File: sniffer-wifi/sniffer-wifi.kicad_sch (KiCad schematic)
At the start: 23 parts, among them J1 Conn_01x05_Pin, J2 Screw_Terminal_01x02, J3 Screw_Terminal_01x02, Q1 BC547, Q2 BC547, Q3 BC547, U1 ESP-12E

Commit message: change schematics
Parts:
- removed J1: Conn_01x05_Pin, Connector_PinHeader_2.54mm:PinHeader_1x05_P2.54mm_Vertical, symbol Connector:Conn_01x05_Pin
- removed Q1, Q2: BC547, Package_TO_SOT_THT:TO-92, symbol Simulation_SPICE:NPN
- added C1: 100n, symbol Device:C
- added C2: 10u, symbol Device:C_Polarized
- added D2, D5: 1N4148, symbol Device:D
- added D3, D4: LED, LED_THT:LED_D3.0mm, symbol Device:LED
- added J1: USB_B_Micro, Connector_USB:USB_Micro-AB_Molex_47590-0001, symbol Connector:USB_B_Micro
- added J5: Conn_01x03_Pin, Connector_PinSocket_2.54mm:PinSocket_1x03_P2.54mm_Vertical, symbol Connector:Conn_01x03_Pin
- added JP1: Jumper_2_Open, TestPoint:TestPoint_2Pads_Pitch5.08mm_Drill1.3mm, symbol Jumper:Jumper_2_Open
- added R16: 1k, symbol Device:R
- added R17: 100, Resistor_THT:R_Axial_DIN0207_L6.3mm_D2.5mm_P7.62mm_Horizontal, symbol Device:R
- added SW1: SW_SPST, Button_Switch_THT:SW_PUSH_6mm_H5mm, symbol Switch:SW_SPST
- added U2: LF33_TO220, Package_TO_SOT_THT:TO-220-3_Vertical, symbol Regulator_Linear:LF33_TO220
- R12, R13: value 10k -> 1k; footprint (none) -> Resistor_THT:R_Axial_DIN0207_L6.3mm_D2.5mm_P7.62mm_Horizontal
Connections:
- net +3V3: now also C2.1, D3.2 (A), D4.2 (A), D5.2 (A), U2.3 (VO); no longer R15.2
- net BOOT: now also JP1.2 (B)
- net GND: now also C1.2, C2.2, D2.2 (A), J1.5 (GND), J1.6 (Shield), J5.3 (Pin_3), JP1.1 (A), SW1.1 (A), U2.2 (GND)
- net L+: now also R17.2; no longer Q3.3 (E)
- net L+TTL: now also D2.1 (K), R16.1; no longer Q3.1 (C), R14.2
- net RESET: now also SW1.2 (B)
- net RX: now also J5.2 (Pin_2)
- net TX: now also J5.1 (Pin_1)
- net STATUS_RED: now reaches R13.2
- net STATUS_RED: now also U1.7 (GPIO13)
- net STATUS_GREEN: now reaches R12.2
- net STATUS_GREEN: now also U1.6 (GPIO12)
- net DTR: no longer names the net of R12.1
- net DTR: now also D3.1 (K)
- net RTS: no longer names the net of R13.1
- net RTS: now also D4.1 (K)
- new net: Q3.1 (C), R14.2, R16.2
- new net: Q3.3 (E), R17.1
- new net: D5.1 (K), R15.2
- new net +5V: C1.1, J1.1 (VBUS), U2.1 (VI)
- no-connect marks 0 -> 4
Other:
- moved on the sheet: Q3, R14, R15

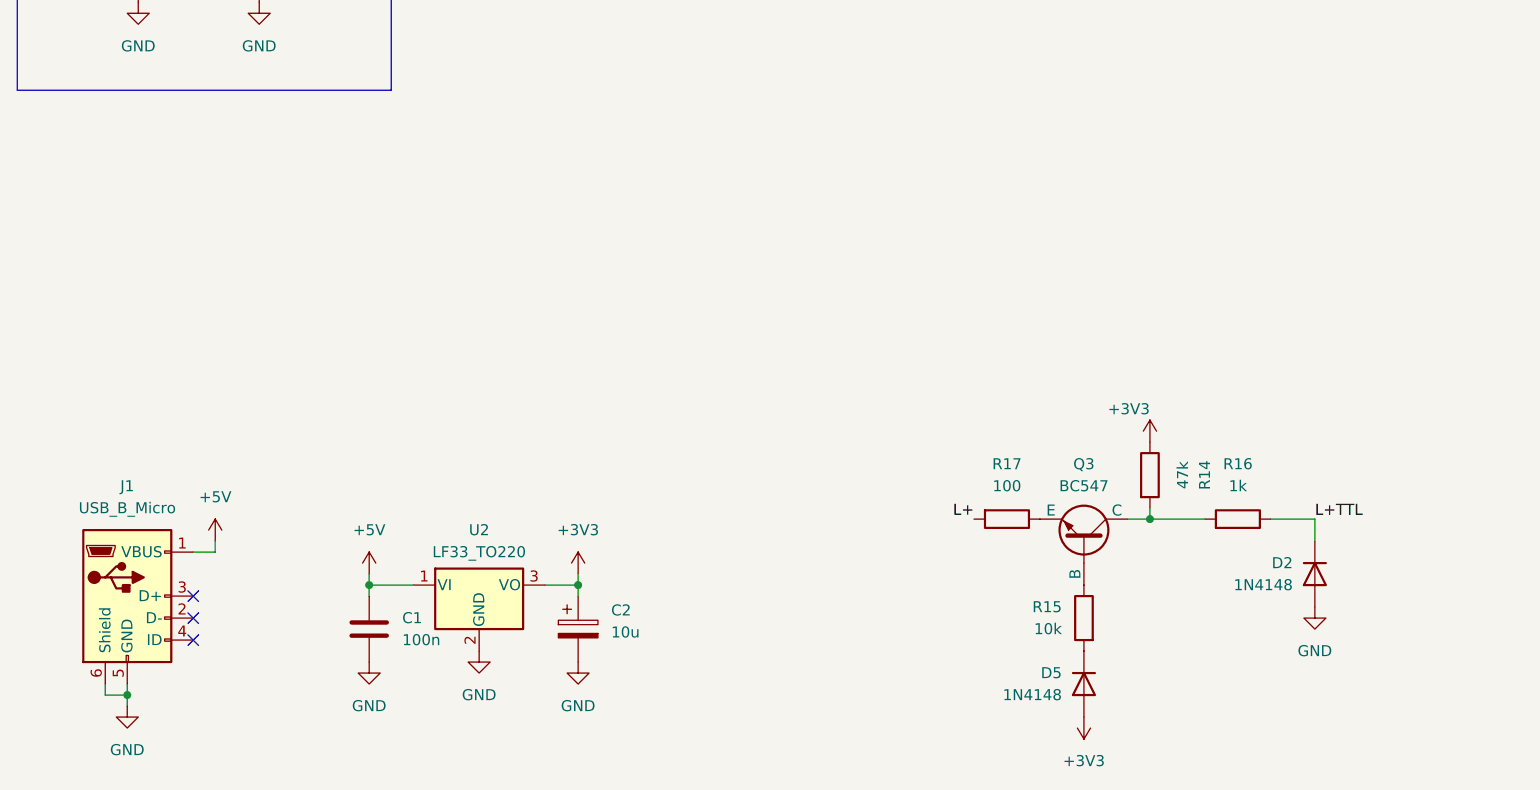
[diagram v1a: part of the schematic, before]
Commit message: modify L+ to LVTTL converter
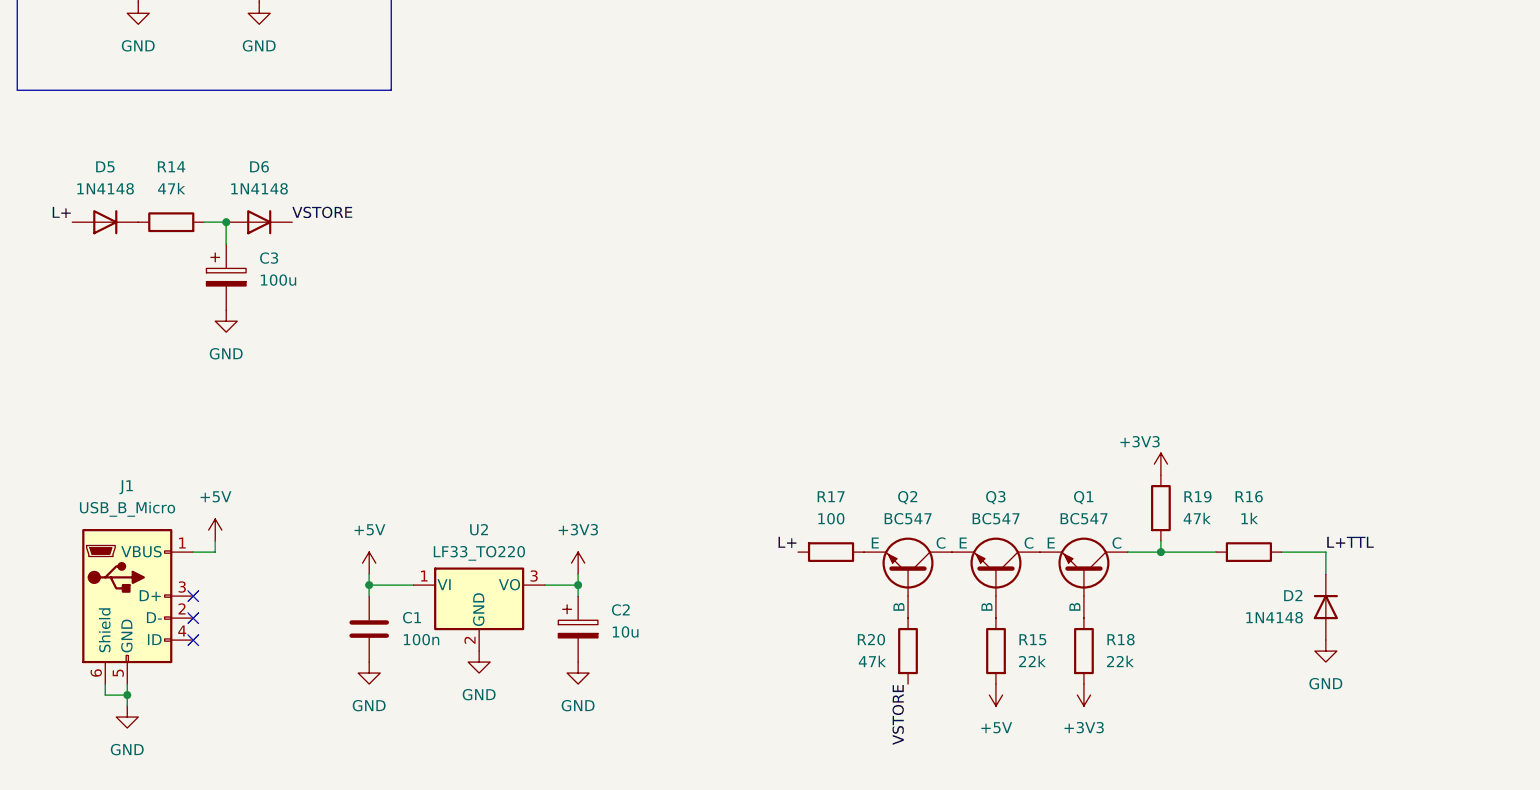
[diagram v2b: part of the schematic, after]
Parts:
- added C3: 100u, symbol Device:C_Polarized
- added D6: 1N4148, symbol Device:D
- added Q1, Q2: BC547, Package_TO_SOT_THT:TO-92, symbol Simulation_SPICE:NPN
- added R18: 22k, symbol Device:R
- added R19, R20: 47k, symbol Device:R
- R15: value 10k -> 22k
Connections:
- net +3V3: now also R18.2, R19.1; no longer D5.2 (A), R14.1
- net +5V: now also R15.2
- net GND: now also C3.2
- net L+: now also D5.2 (A)
- net at Q3.3 (E): now also Q2.1 (C); no longer R17.1
- net at D5.1 (K): now also R14.1; no longer R15.2
- new net: Q1.3 (E), Q3.1 (C)
- new net: Q1.1 (C), R16.2, R19.2
- new net: Q1.2 (B), R18.1
- new net: C3.1, D6.2 (A), R14.2
- new net: Q2.2 (B), R20.1
- new net: Q2.3 (E), R17.1
- new net VSTORE: D6.1 (K), R20.2
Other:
- moved on the sheet: D2, Q3, R15, R16, R17

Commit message: major hw redesign
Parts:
- removed C3: 100u, symbol Device:C_Polarized
- removed D5, D6: 1N4148, symbol Device:D
- removed J5: Conn_01x03_Pin, Connector_PinSocket_2.54mm:PinSocket_1x03_P2.54mm_Vertical, symbol Connector:Conn_01x03_Pin
- removed JP1: Jumper_2_Open, TestPoint:TestPoint_2Pads_Pitch5.08mm_Drill1.3mm, symbol Jumper:Jumper_2_Open
- removed R11, R3, R5, R7, R9: 1M, symbol Device:R
- removed SW1: SW_SPST, Button_Switch_THT:SW_PUSH_6mm_H5mm, symbol Switch:SW_SPST
- removed U1: ESP-12E, RF_Module:ESP-12E, symbol RF_Module:ESP-12E
- added C1, C5: 22p, symbol Device:C
- added C2: 100u, symbol Device:C_Polarized
- added C3, C4, C6: 100n, symbol Device:C
- added C9: 10n, symbol Device:C
- added D2: 9V1, symbol Device:D_Zener
- added J2: Conn_01x05_Socket, Connector_PinHeader_2.54mm:PinHeader_1x05_P2.54mm_Vertical, symbol Connector:Conn_01x05_Socket
- added J5: Conn_02x04_Odd_Even, Connector_PinSocket_2.54mm:PinSocket_2x04_P2.54mm_Vertical, symbol Connector_Generic:Conn_02x04_Odd_Even
- added R13, R16: 100, symbol Device:R
- added R15, R21: 10k, symbol Device:R
- added R17: 10M 1%, symbol Device:R
- added R19: 1M 1%, symbol Device:R
- added U1: ATmega328PB-A, Package_QFP:TQFP-32_7x7mm_P0.8mm, symbol MCU_Microchip_ATmega:ATmega328PB-A
- added Y1: 16 MHz, symbol Device:Crystal
- R1: value 470k -> 100
- R10, R2, R4, R6, R8: value 1M -> 10k
- R14, R20: value 47k -> 10k
- R18: value 22k -> 10M 1%
- R3: renamed from R17; value 100 -> 100k
- R5: renamed from R15; value 22k -> 100k
- R9: renamed from R19; value 47k -> 100k
- renumbered C1 to C7, C2 to C8, D2 to D3, D3 to D4, D4 to D5, J2 to J3, J3 to J4, R12 to R11, R13 to R12, R16 to R7
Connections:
- net VSTORE is gone; now on net +3V3: R20.2
- net +3V3: now also R10.1, R14.2, R4.1, R6.1, R8.1, J5.1 (Pin_1), R21.1; no longer R18.2, R9.1
- net +5V: now also R1.2, R2.1, R9.1, C2.1, C4.1, R15.1, U1.4 (VCC)
- net ADC: now also R18.2, C9.1, R19.1, U1.23 (PC0); no longer D1.1 (K), R1.1, R2.2
- net GND: now also C1.2, C2.2, C3.2, C4.2, C5.2, C6.2, C9.2, D2.2 (A), J2.4 (Pin_4), J5.8 (Pin_8), R19.2, U1.21 (GND), U1.5 (GND); no longer D1.2 (A), R1.2
- net L+: now also D1.1 (K), R17.1
- net L+TTL: now also R9.2, U1.1 (PD3), U1.32 (PD2)
- net RESET: now also R2.2, J2.2 (Pin_2), U1.29 (~{RESET}/PC6)
- net RXD: now also Q2.1 (C), R15.2, U1.30 (PD0)
- net STATUS_GREEN: now also U1.12 (PB0)
- net STATUS_RED: now also U1.13 (PB1)
- net TXD: now also R16.1, U1.31 (PD1)
- net at Q1.3 (E): now also D1.2 (A), R3.1, D2.1 (K); no longer Q3.1 (C)
- net at Q3.2 (B): now also R20.1; no longer R5.1
- net at Q3.3 (E): now also R16.2; no longer Q2.1 (C)
- net GPIO0: now reaches R8.2
- net GPIO0: now also J5.4 (Pin_4)
- net CH_PD: now reaches R6.2
- net CH_PD: now also J5.5 (Pin_5)
- net at R14.1: now also Q2.2 (B)
- net ESP_RESET: now reaches R4.2
- net ESP_RESET: now also J5.3 (Pin_3)
- net at Q1.1 (C), R7.2: no longer R9.2
- net at Q1.2 (B): now also R5.1; no longer R18.1
- net at Q2.3 (E): now also R13.2; no longer R3.1
- net GPIO2: now reaches R10.2
- net GPIO2: now also J5.6 (Pin_6)
- new net: C6.1, U1.20 (AREF)
- new net: R17.2, R18.1
- new net AVCC: C3.1, R1.1, U1.18 (AVCC)
- new net ESP_RX: J5.2 (Pin_2), Q3.1 (C), R21.2
- new net ESP_TX: J5.7 (Pin_7), R13.1
- new net MISO: J2.3 (Pin_3), U1.16 (PB4)
- new net MOSI: J2.1 (Pin_1), U1.15 (PB3)
- new net SCK: J2.5 (Pin_5), U1.17 (PB5)
- new net XTAL1: C1.1, U1.7 (XTAL1/PB6), Y1.1
- new net XTAL2: C5.1, U1.8 (XTAL2/PB7), Y1.2
- no-connect marks 4 -> 17
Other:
- note removed: "ADC Vref = 1.1 V"
- company: Omnivid -> Evil Corp.
- title: Proel sniffer -> Doorphone sniffer
- moved on the sheet: D3, J3, J4, Q1, R3, R5, R7, R9

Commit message: add protection diode for adc
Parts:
- added D6: 1N4148, symbol Device:D
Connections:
- net ADC: now also D6.1 (K)
- net GND: now also D6.2 (A)
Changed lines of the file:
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@@
 	)
 	(junction
+		(at 256.54 77.47)
+		(diameter 0)
+		(color 0 0 0 0)
+	)
+	(junction
 		(at 22.86 77.47)
 		(diameter 0)
@@
 	(wire
 		(pts
+			(xy 246.38 78.74) (xy 246.38 77.47)
+		)
+		(stroke
+			(width 0)
+			(type default)
+		)
+	)
+	(wire
+		(pts
 			(xy 80.01 170.18) (xy 80.01 171.45)
 		)
@@
 	(wire
 		(pts
+			(xy 246.38 77.47) (xy 256.54 77.47)
+		)
+		(stroke
+			(width 0)
+			(type default)
+		)
+	)
+	(wire
+		(pts
 			(xy 256.54 77.47) (xy 261.62 77.47)
 		)
@@
 	)
 	(symbol
+		(lib_id "Device:D")
+		(at 246.38 82.55 270)
+		(unit 1)
+		(exclude_from_sim no)
+		(in_bom yes)
+		(on_board yes)
+		(dnp no)
+		(property "Reference" "D6"
+			(at 243.84 81.2799 90)
+			(effects
+				(font
+					(size 1.27 1.27)
+				)
+				(justify right)
+			)
+		)
+		(property "Value" "1N4148"
+			(at 243.84 83.8199 90)
+			(effects
+				(font
+					(size 1.27 1.27)
+				)
+				(justify right)
+			)
+		)
+		(property "Footprint" ""
+			(at 246.38 82.55 0)
+			(effects
+				(font
+					(size 1.27 1.27)
+				)
+				(hide yes)
+			)
+		)
+		(property "Datasheet" "~"
+			(at 246.38 82.55 0)
+			(effects
+				(font
+					(size 1.27 1.27)
+				)
+				(hide yes)
+			)
+		)
+		(property "Description" "Diode"
+			(at 246.38 82.55 0)
+			(effects
+				(font
+					(size 1.27 1.27)
+				)
+				(hide yes)
+			)
+		)
+		(property "Sim.Device" "D"
+			(at 246.38 82.55 0)
+			(effects
+				(font
+					(size 1.27 1.27)
+				)
+				(hide yes)
+			)
+		)
+		(property "Sim.Pins" "1=K 2=A"
+			(at 246.38 82.55 0)
+			(effects
+				(font
+					(size 1.27 1.27)
+				)
+				(hide yes)
+			)
+		)
+		(pin "2"
+		)
+		(pin "1"
+		)
+		(instances
+			(project ""
+				(path "/db70fe1b-d2b4-43f9-a78d-d9b71a224de5"
+					(reference "D6")
+					(unit 1)
+				)
+			)
+		)
+	)
+	(symbol
 		(lib_id "Device:C_Polarized")
 		(at 80.01 176.53 0)
@@
 					(unit 1)
 				)
+			)
+		)
+	)
+	(symbol
+		(lib_id "power:GND")
+		(at 246.38 86.36 0)
+		(unit 1)
+		(exclude_from_sim no)
+		(in_bom yes)
+		(on_board yes)
+		(dnp no)
+		(fields_autoplaced yes)
+		(property "Reference" "#PWR039"
+			(at 246.38 92.71 0)
+			(effects
+				(font
+					(size 1.27 1.27)
+				)
+				(hide yes)
+			)
+		)
+		(property "Value" "GND"
+			(at 246.38 91.44 0)
+			(effects
+				(font
+					(size 1.27 1.27)
+				)
+			)
+		)
+		(property "Footprint" ""
+			(at 246.38 86.36 0)
+			(effects
+				(font
+					(size 1.27 1.27)
+				)
+				(hide yes)
+			)
+		)
+		(property "Datasheet" ""
+			(at 246.38 86.36 0)
+			(effects
+				(font
+					(size 1.27 1.27)
+				)
+				(hide yes)
+			)
+		)
+		(property "Description" "Power symbol creates a global label with name \"GND\" , ground"
+			(at 246.38 86.36 0)
+			(effects
+				(font
+					(size 1.27 1.27)
+				)
+				(hide yes)
+			)
+		)
+		(pin "1"
+		)
+		(instances
+			(project ""
+				(path "/db70fe1b-d2b4-43f9-a78d-d9b71a224de5"
+					(reference "#PWR039")
+					(unit 1)
+				)

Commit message: add filtering capacitor, change crystal to fit UART requirements
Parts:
- added C10: 1n, symbol Device:C
- Y1: value 16 MHz -> 18.4320 MHz
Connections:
- net GND: now also C10.2
- net L+TTL: now also C10.1
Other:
- moved on the sheet: D1, D2, D3, Q1, R3, R5, R7, R9
